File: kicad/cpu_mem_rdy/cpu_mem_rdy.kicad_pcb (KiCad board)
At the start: 2 copper layers, 160 x 100.3 mm, 68 parts, among them P1 CONN_02X04, P2 CONN_01X08, P3 CONN_01X03, P4 CONN_02X02, P5 CONN_02X25, P6 POWER, SW1 SW_PUSH, U1 W65C02SP, U11 74LS273, U12 74LS244, U14 GAL16V8, U2 LM555N, U3 74HCT00, U4 74LS393, U5 GAL22V10, U6 28C256, U7 HM62256BLP-7, U8 HM62256BLP-7, U9 74LS139, X1 OSC

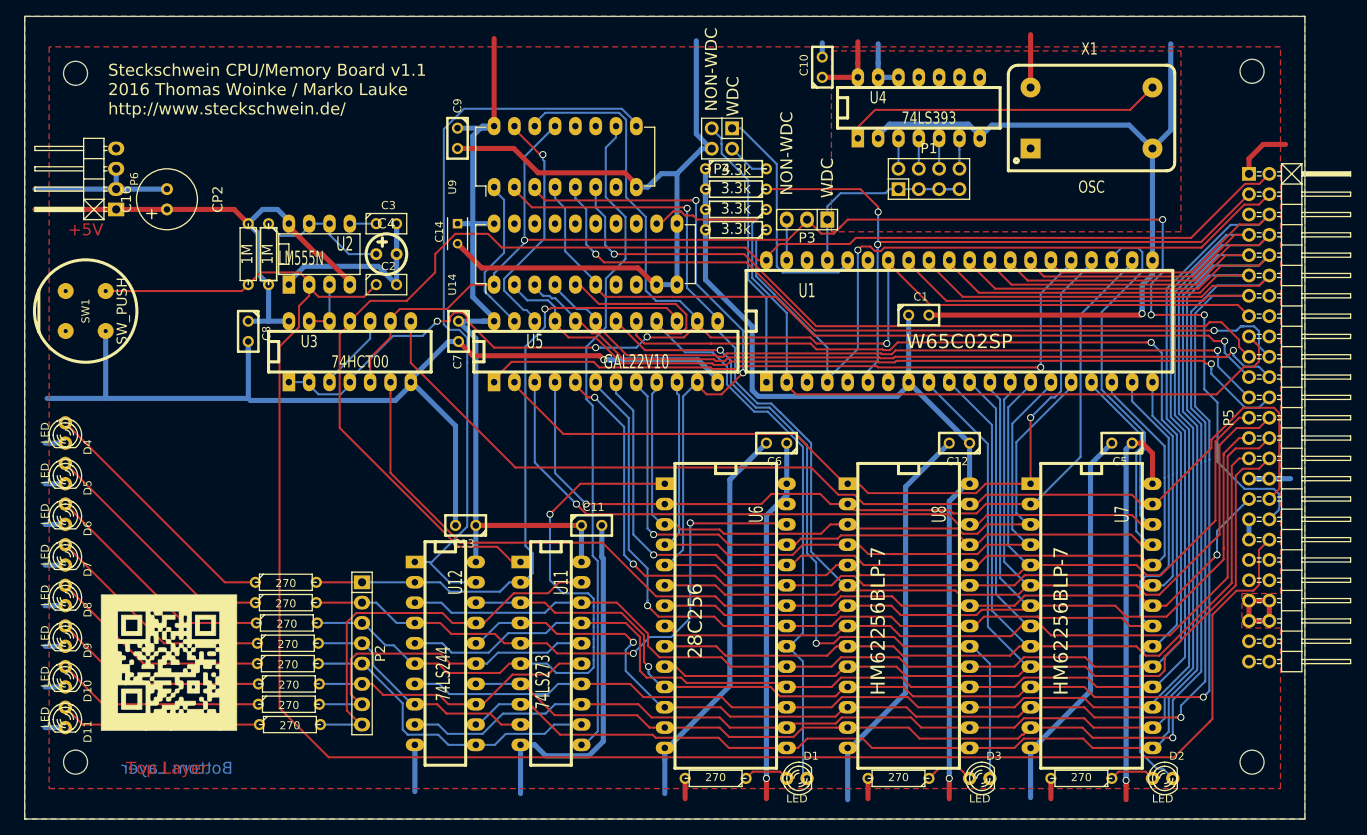
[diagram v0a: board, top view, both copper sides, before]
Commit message: cleanup routing, micro usb jack
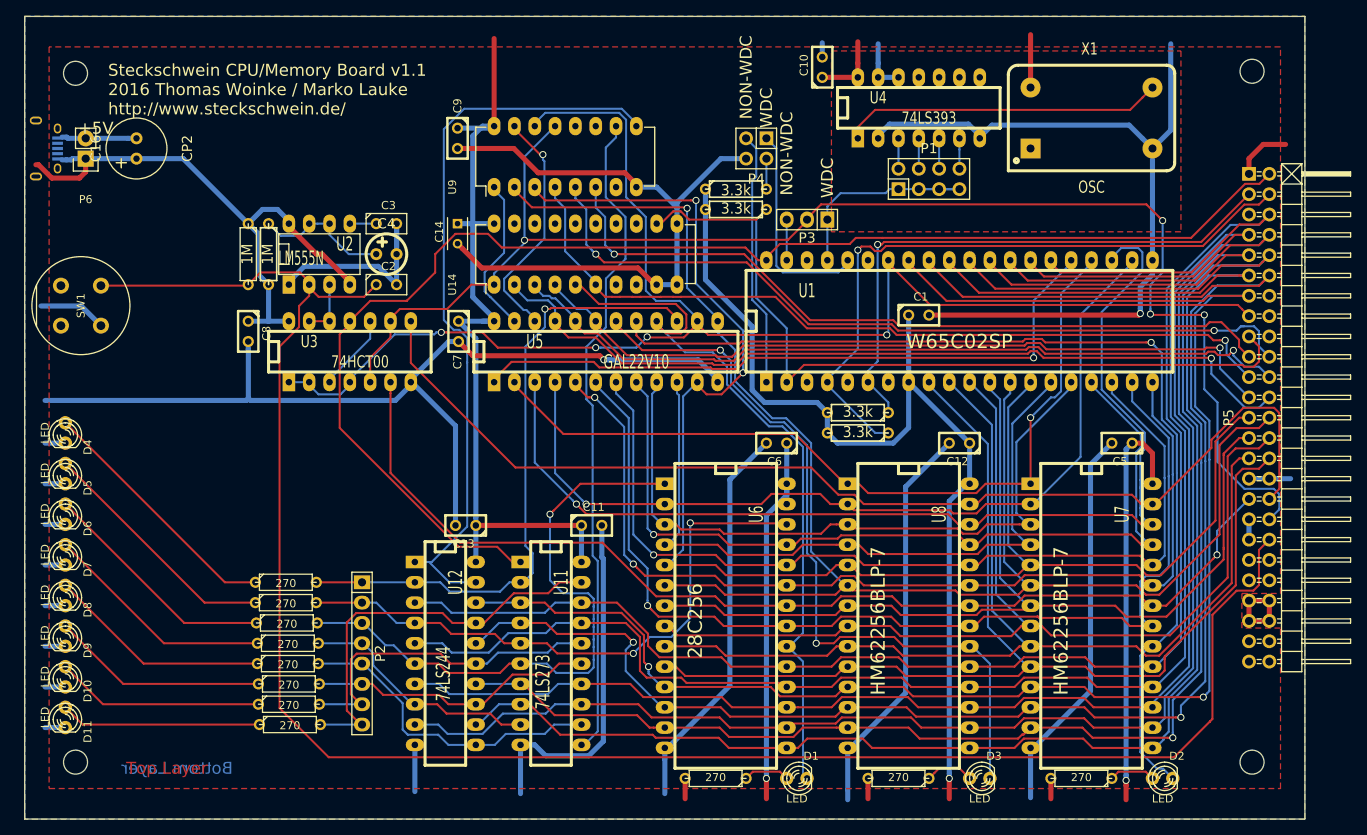
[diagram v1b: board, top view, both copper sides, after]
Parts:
- removed G***: LOGO, Steckschwein:QRCODE
- added CON1: USB-MICRO-B, Connect:USB_Micro-B, B.Cu at (64.8, 62.2)
- P6: footprint Pin_Headers:Pin_Header_Angled_1x04 -> Pin_Headers:Pin_Header_Straight_1x02
- SW1: footprint Discret:PUSH_BUTT_SHAPE1 -> Buttons_Switches_ThroughHole:Push_E-Switch_KS01Q01
- moved R2 31.8 mm to (166.4, 95.2)
- moved R1 29.6 mm to (166.4, 97.8)
- moved C16 7.41 mm to (76.2, 63.5)
- moved P6 4.58 mm to (69.8, 63.5), turned to 180 degrees
- moved P4 4.47 mm to (153.7, 62.2)
- moved SW1 3.70 mm to (71.8, 79.4)
- moved R4 2.54 mm to (151.1, 67.3)
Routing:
- net GND: track 600.7 -> 579.1 mm
- net /NMI: track 86.9 -> 72.1 mm, vias 2 -> 1
- net VCC: track 425.0 -> 437.5 mm
- net /IRQ: track 96.1 -> 83.7 mm
- net /RW: track 188.3 -> 184.1 mm
- net Net-(P4-Pad1): track 30.6 -> 27.0 mm
- net Net-(P4-Pad3): track 34.5 -> 32.0 mm
- net RDY: track 104.8 -> 103.1 mm
- net Net-(P4-Pad2): track 5.33 -> 3.81 mm
- net /decoder/A15: track 85.1 -> 83.8 mm
- net /CS_VDP: track 103.9 -> 105.3 mm
- net /CS_UART: track 95.3 -> 96.5 mm
- net /CS_VIA: track 98.6 -> 99.7 mm

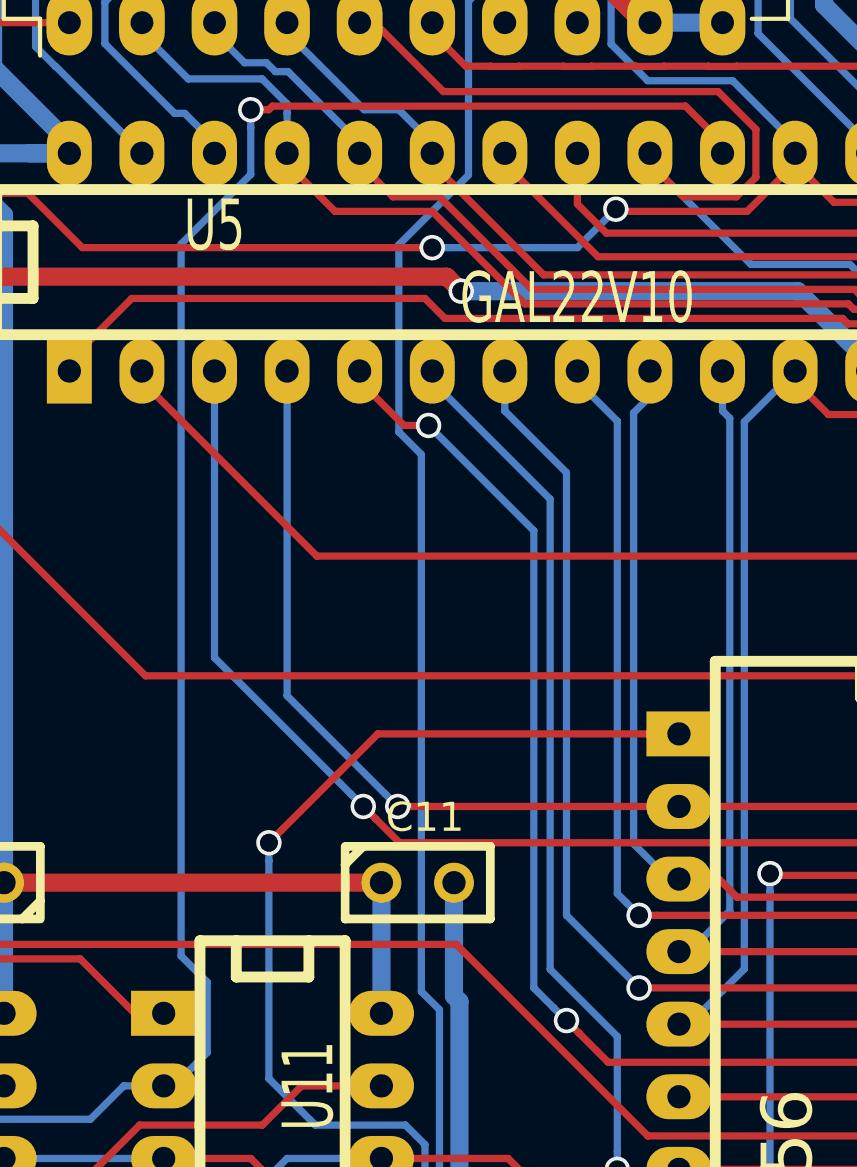
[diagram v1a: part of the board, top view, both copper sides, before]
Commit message: one via less
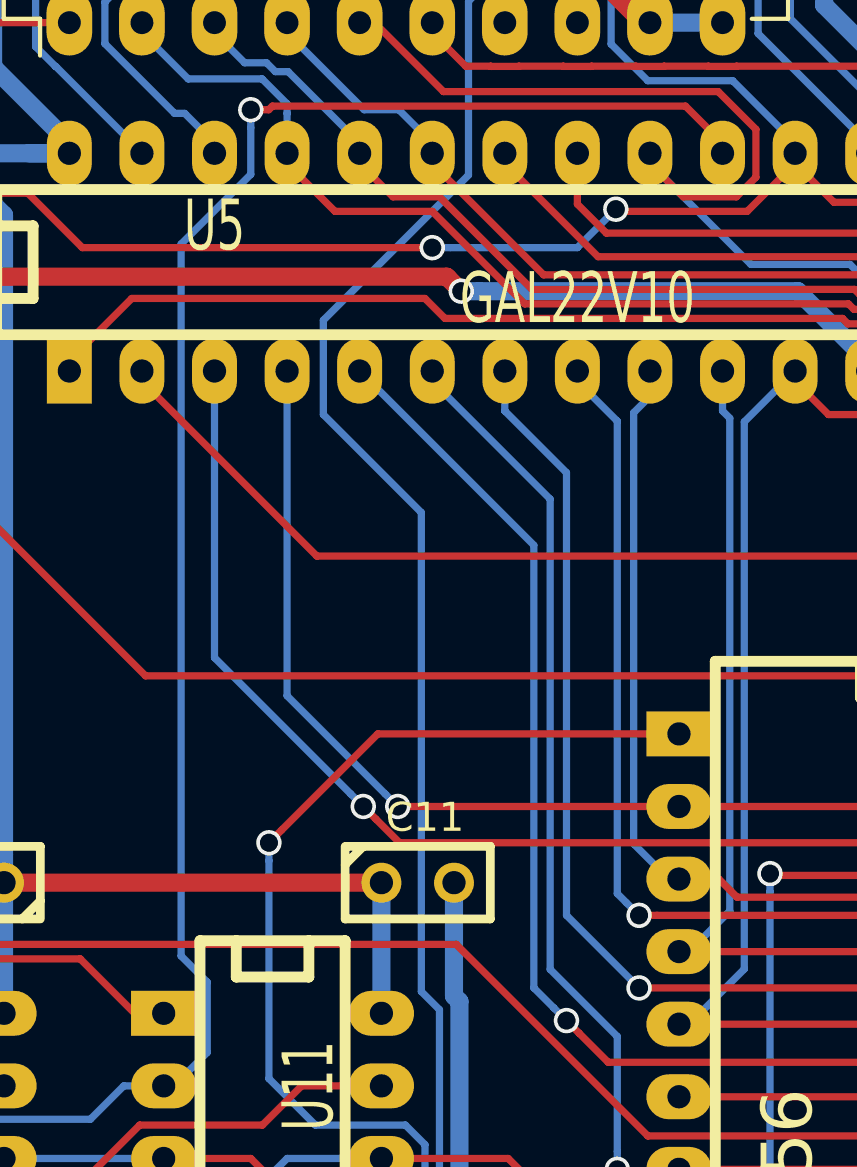
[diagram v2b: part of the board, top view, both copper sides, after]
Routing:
- net Net-(U11-Pad11): track 82.6 -> 84.7 mm
- net /decoder/A11: track 124.0 -> 123.9 mm, vias 2 -> 1

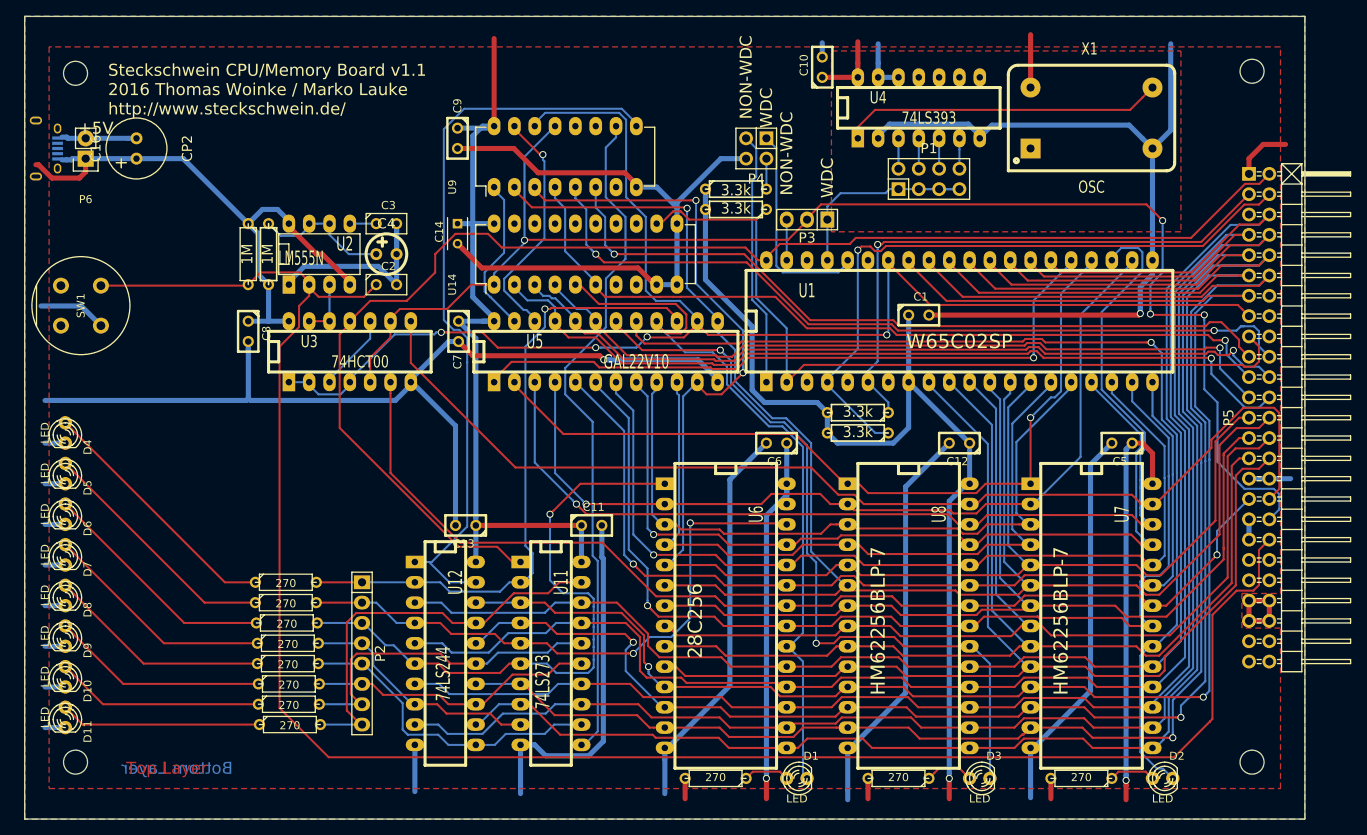
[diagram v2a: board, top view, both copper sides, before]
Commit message: new footprints from current library, much nicer routing of memory area
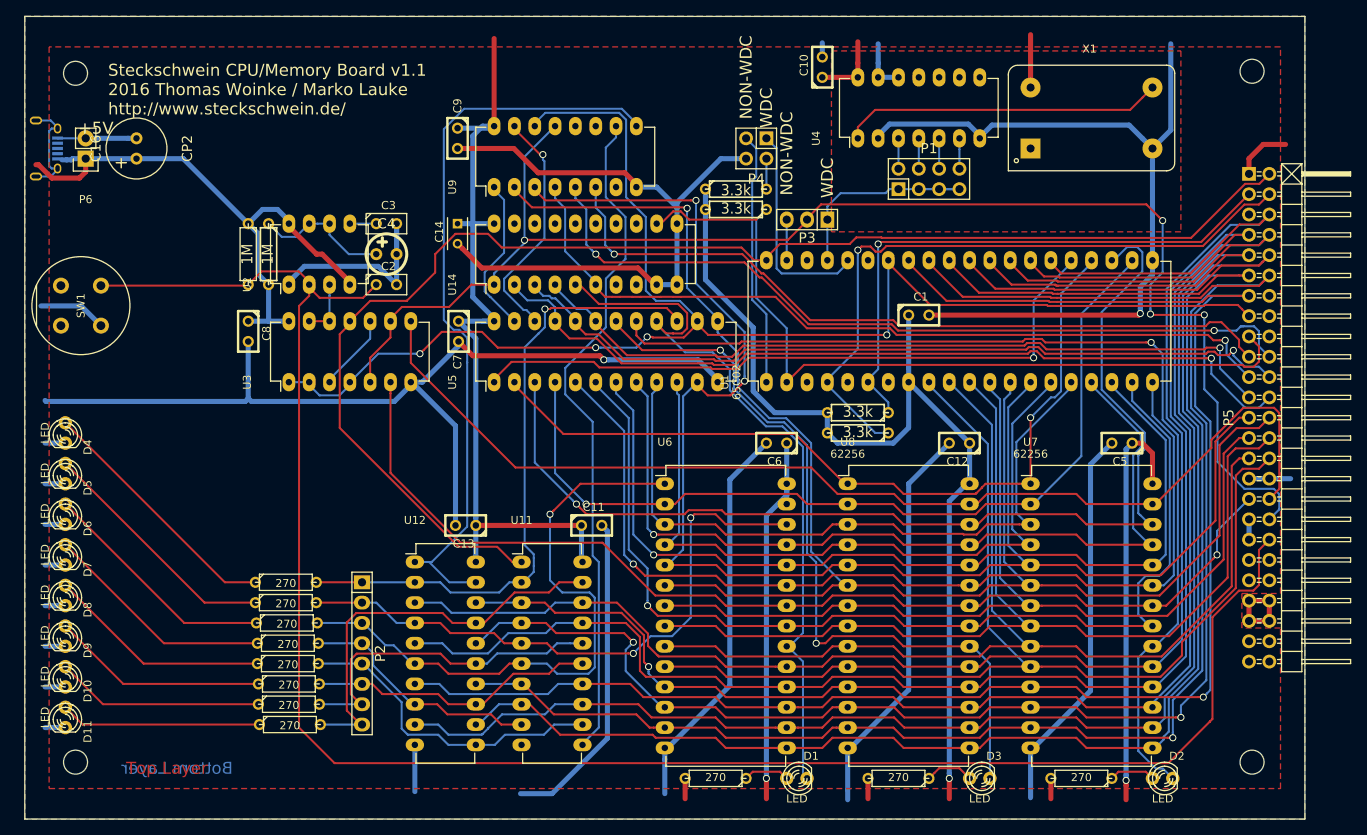
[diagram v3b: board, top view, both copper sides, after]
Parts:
- U1: value W65C02SP -> 65C02; footprint Sockets_DIP:DIP-40__600_ELL -> Housings_DIP:DIP-40_W15.24mm_LongPads
- U11, U12: footprint Sockets_DIP:DIP-20__300_ELL -> Housings_DIP:DIP-20_W7.62mm_LongPads
- U2: footprint Sockets_DIP:DIP-8__300_ELL -> Housings_DIP:DIP-8_W7.62mm_LongPads
- U3, U4: footprint Sockets_DIP:DIP-14__300_ELL -> Housings_DIP:DIP-14_W7.62mm_LongPads
- U5: footprint Sockets_DIP:DIP-24__300_ELL -> Housings_DIP:DIP-24_W7.62mm_LongPads
- U6: footprint Sockets_DIP:DIP-28__600_ELL -> Housings_DIP:DIP-28_W15.24mm_LongPads
- U7, U8: value HM62256BLP-7 -> 62256; footprint Sockets_DIP:DIP-28__600_ELL -> Housings_DIP:DIP-28_W15.24mm_LongPads
- X1: footprint Oscillator-Modules:OSCILLATOR_KXO-200_LargePads -> Oscillators:KXO-200_LargePads
- moved U1 25.3 mm to (154.9, 91.4), turned to 90 degrees
- moved U6 18.2 mm to (142.2, 104.1), turned to 0 degrees
- moved U7 18.2 mm to (188.0, 104.1), turned to 0 degrees
- moved U8 18.2 mm to (165.1, 104.1), turned to 0 degrees
- moved U5 14.5 mm to (120.9, 91.4), turned to 90 degrees
- moved U12 12.0 mm to (111.0, 113.9), turned to 0 degrees
- moved U11 12.0 mm to (124.3, 113.9), turned to 0 degrees
- moved U3 8.52 mm to (95.2, 91.4), turned to 90 degrees
- moved U4 8.52 mm to (166.4, 61.0), turned to 90 degrees
- moved U2 5.39 mm to (95.2, 79.2), turned to 90 degrees
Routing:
- net Net-(CON1-Pad6): track 0.00 -> 13.1 mm
- net GND: track 579.1 -> 575.8 mm
- net /Connector/RESET_TRIG: track 240.0 -> 238.3 mm
- net /Connector/A5: track 193.5 -> 194.5 mm
- net /decoder/BANK1: track 75.6 -> 76.5 mm
- net /decoder/A13: track 136.1 -> 136.7 mm
- net /decoder//CS_ROM: track 92.3 -> 92.8 mm
- net /decoder/BANK2: track 78.1 -> 78.6 mm
- net /decoder/A11: track 123.9 -> 123.3 mm

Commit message: touch up
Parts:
- SW1: value SW_PUSH -> RESET
- U11: value 74LS273 -> 74HCT273
- U12: value 74LS244 -> 74HCT244
- U2: value LM555N -> NE555
- U4: value 74LS393 -> 74HCT393
- U9: value 74LS139 -> 74HCT139
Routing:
- net /decoder/A14: track 103.2 -> 108.8 mm
- net /Connector/A5: track 194.5 -> 191.7 mm
- net Net-(U12-Pad1): track 94.9 -> 92.5 mm
- net /decoder/A13: track 136.7 -> 138.1 mm
- net /Connector/D1: track 211.5 -> 210.2 mm
- net PHI2: track 181.3 -> 180.2 mm
- net /decoder//CS_HIRAM: track 95.4 -> 94.4 mm, vias 2 -> 1
- net /CS_VDP: track 105.3 -> 104.3 mm
- net /CS_UART: track 96.5 -> 95.6 mm
- net /Connector/D7: track 197.9 -> 197.2 mm
- net /Connector/A1: track 132.2 -> 131.5 mm
- net /Connector/D6: track 198.3 -> 197.6 mm
- net /Connector/A2: track 131.2 -> 130.5 mm
- net /RW: track 184.2 -> 184.8 mm
- net /Connector/A4: track 201.5 -> 200.9 mm
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
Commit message: touch up 2
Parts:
- moved C12 1.27 mm to (179.1, 100.3)
- moved C5 1.27 mm to (199.4, 100.3)
- moved C6 1.27 mm to (156.2, 100.3)
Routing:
- net GND: track 576.1 -> 572.3 mm
- net VCC: track 437.6 -> 440.0 mm
- net /CS_IO0: track 101.7 -> 102.9 mm
- net /Connector/A4: track 200.9 -> 199.9 mm
- net /decoder//CS_HIRAM: track 94.4 -> 93.4 mm
- net /decoder//CS_ROM: track 92.4 -> 91.5 mm
